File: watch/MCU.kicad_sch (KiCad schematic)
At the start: 14 parts, among them IC601 FAN5622SX, IC602 USBLC6-2P6, IC603 MX25U51245GZ4I00, IC604 NTS0104GU12, M601 NORA-B106, X603 Device, X608 Display

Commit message: Add speaker
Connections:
- net BMI270-INT: now also M601.E7 (P0.06/AIN2); no longer M601.G1 (P1.06)
- net LIS2MDL-INT: now also M601.F7 (P1.07); no longer M601.H7 (P0.29)
- net MIC-CLK: now also M601.G3 (P0.25/AIN4); no longer M601.F8 (P1.14)
- net MIC-DATA: now also M601.G2 (P0.26/AIN5); no longer M601.F9 (P1.15)
- net PA-BCLK: now also M601.C8 (P0.22); no longer M601.E7 (P0.06/AIN2)
- net Status: now also M601.E3 (P0.21); no longer M601.D3 (P0.07/AIN3)
- net VIB-EN: now also M601.G1 (P1.06); no longer M601.G2 (P0.26/AIN5)
- net ~{RESET_{HR}}: now also M601.D3 (P0.07/AIN3); no longer M601.E3 (P0.21)
- net ~{RTC-INT}: now also M601.F9 (P1.15); no longer M601.C8 (P0.22)
- no-connect marks 12 -> 10
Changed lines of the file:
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@@
 	)
 	(no_connect
-		(at 153.67 77.47)
-	)
-	(no_connect
-		(at 231.14 124.46)
-	)
-	(no_connect
 		(at 231.14 132.08)
 	)
@@
 	(wire
 		(pts
-			(xy 231.14 106.68) (xy 232.41 106.68)
+			(xy 153.67 77.47) (xy 154.94 77.47)
 		)
 		(stroke
@@
 	(wire
 		(pts
-			(xy 153.67 85.09) (xy 154.94 85.09)
+			(xy 231.14 104.14) (xy 232.41 104.14)
 		)
 		(stroke
@@
 	(wire
 		(pts
-			(xy 231.14 127) (xy 232.41 127)
+			(xy 153.67 125.73) (xy 154.94 125.73)
 		)
 		(stroke
@@
 	(wire
 		(pts
-			(xy 154.94 67.31) (xy 153.67 67.31)
+			(xy 232.41 124.46) (xy 231.14 124.46)
 		)
 		(stroke
@@
 	(wire
 		(pts
-			(xy 153.67 125.73) (xy 154.94 125.73)
+			(xy 153.67 85.09) (xy 154.94 85.09)
 		)
 		(stroke
@@
 	(wire
 		(pts
+			(xy 231.14 127) (xy 232.41 127)
+		)
+		(stroke
+			(width 0)
+			(type default)
+		)
+	)
+	(wire
+		(pts
 			(xy 109.22 106.68) (xy 109.22 109.22)
 		)
@@
 	(wire
 		(pts
-			(xy 231.14 104.14) (xy 232.41 104.14)
-		)
-		(stroke
-			(width 0)
-			(type default)
-		)
-	)
-	(wire
-		(pts
 			(xy 215.9 187.96) (xy 215.9 193.04)
 		)
@@
 	(hierarchical_label "PA-BCLK"
 		(shape output)
-		(at 154.94 125.73 0)
+		(at 154.94 85.09 0)
 		(effects
 			(font
@@
 	(hierarchical_label "MIC-DATA"
 		(shape input)
-		(at 232.41 104.14 0)
+		(at 154.94 74.93 0)
 		(effects
 			(font
@@
 	(hierarchical_label "~{RTC-INT}"
 		(shape input)
-		(at 154.94 85.09 0)
+		(at 232.41 104.14 0)
 		(effects
 			(font
@@
 	(hierarchical_label "~{RESET_{HR}}"
 		(shape output)
-		(at 154.94 87.63 0)
+		(at 154.94 123.19 0)
 		(effects
 			(font
@@
 	(hierarchical_label "Status"
 		(shape input)
-		(at 154.94 123.19 0)
+		(at 154.94 87.63 0)
 		(effects
 			(font
@@
 	(hierarchical_label "BMI270-INT"
 		(shape input)
-		(at 232.41 127 0)
+		(at 154.94 125.73 0)
 		(effects
 			(font
@@
 	(hierarchical_label "MIC-CLK"
 		(shape output)
-		(at 232.41 106.68 0)
+		(at 154.94 77.47 0)
 		(effects
 			(font
@@
 	(hierarchical_label "LIS2MDL-INT"
 		(shape input)
-		(at 154.94 67.31 0)
+		(at 232.41 124.46 0)
 		(effects
 			(font
@@
 	(hierarchical_label "VIB-EN"
 		(shape output)
-		(at 154.94 74.93 0)
+		(at 232.41 127 0)
 		(effects
 			(font

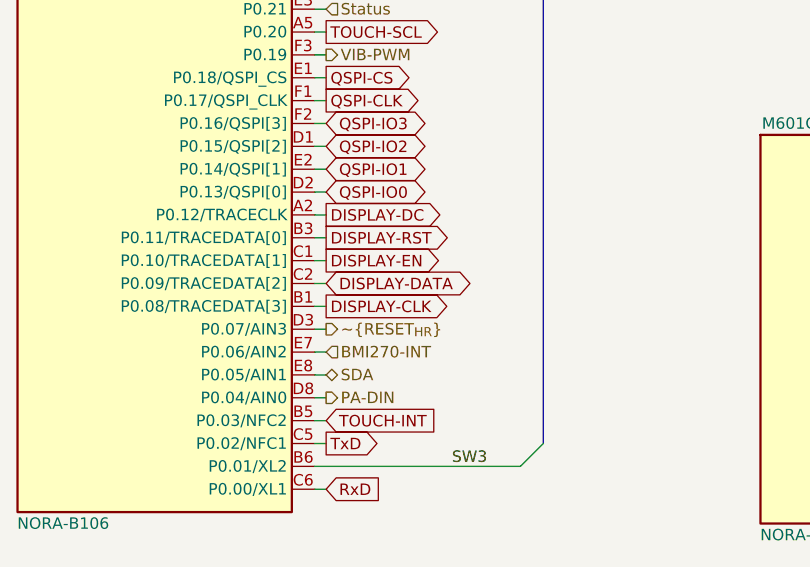
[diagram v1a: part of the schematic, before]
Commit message: Move display connector 3 mm to the outside and optimize routing
Signed-off-by: Daniel Kampert <DanielKampert@kampis-elektroecke.de>
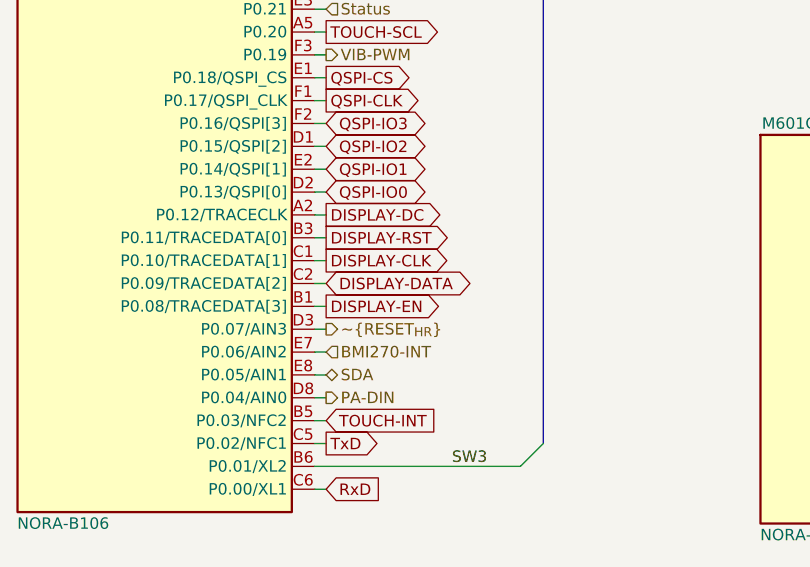
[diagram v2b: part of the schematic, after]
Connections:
- net DISPLAY-CLK: now also M601.C1 (P0.10/TRACEDATA[1]); no longer M601.B1 (P0.08/TRACEDATA[3])
- net DISPLAY-EN: now also M601.B1 (P0.08/TRACEDATA[3]); no longer M601.C1 (P0.10/TRACEDATA[1])
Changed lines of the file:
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@@
 	(global_label "DISPLAY-CLK"
 		(shape output)
-		(at 154.94 120.65 0)
-		(fields_autoplaced yes)
-		(effects
-			(font
-				(size 1.27 1.27)
-			)
-			(justify left)
-		)
-		(property "Intersheetrefs" "${INTERSHEET_REFS}"
-			(at 170.6253 120.65 0)
+		(at 154.94 115.57 0)
+		(fields_autoplaced yes)
+		(effects
+			(font
+				(size 1.27 1.27)
+			)
+			(justify left)
+		)
+		(property "Intersheetrefs" "${INTERSHEET_REFS}"
+			(at 170.6253 115.57 0)
 			(effects
 				(font
@@
 	(global_label "DISPLAY-EN"
 		(shape output)
-		(at 154.94 115.57 0)
-		(fields_autoplaced yes)
-		(effects
-			(font
-				(size 1.27 1.27)
-			)
-			(justify left)
-		)
-		(property "Intersheetrefs" "${INTERSHEET_REFS}"
-			(at 169.5367 115.57 0)
-			(effects
-				(font
+		(at 154.94 120.65 0)
+		(fields_autoplaced yes)
+		(effects
+			(font
+				(size 1.27 1.27)
+			)
+			(justify left)
+		)
+		(property "Intersheetrefs" "${INTERSHEET_REFS}"
+			(at 169.5367 120.65 0)
+			(effects
+				(font

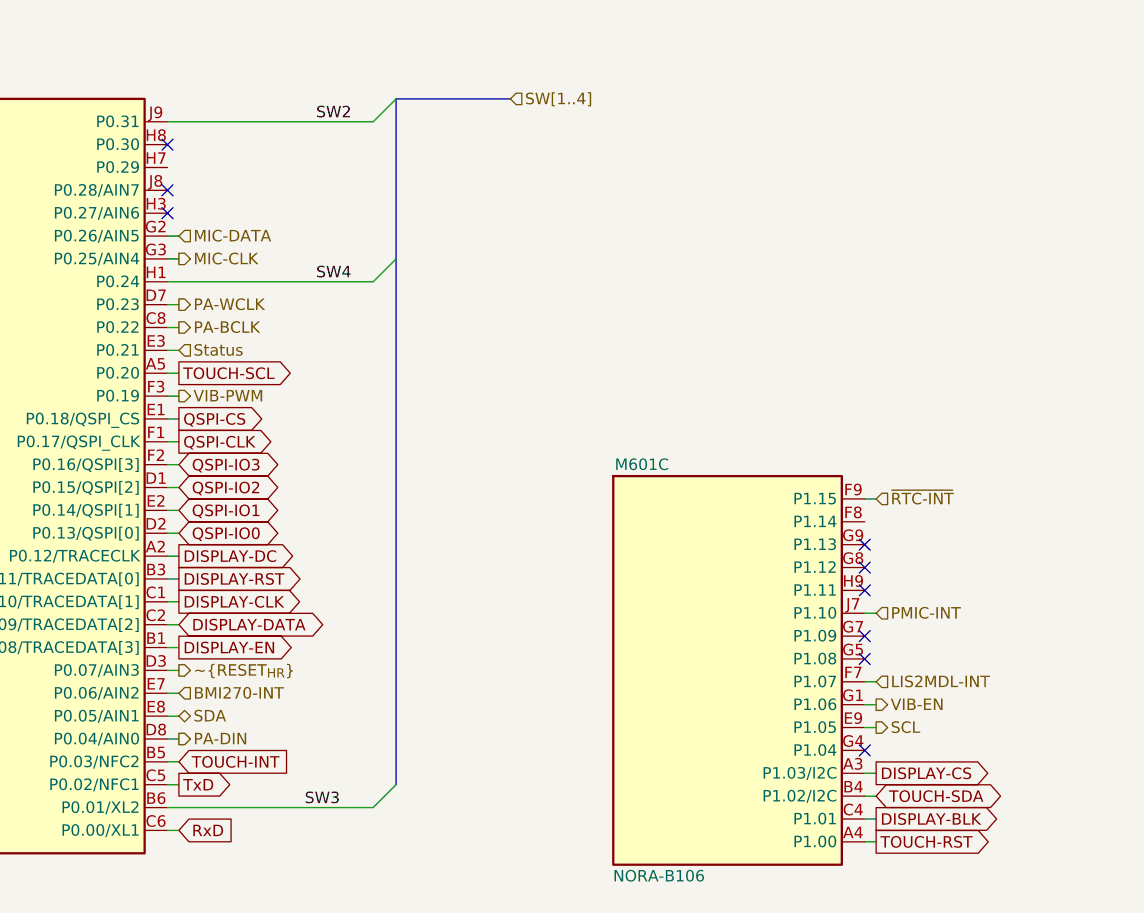
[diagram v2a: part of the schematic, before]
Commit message: Fix wrong Extension footprint
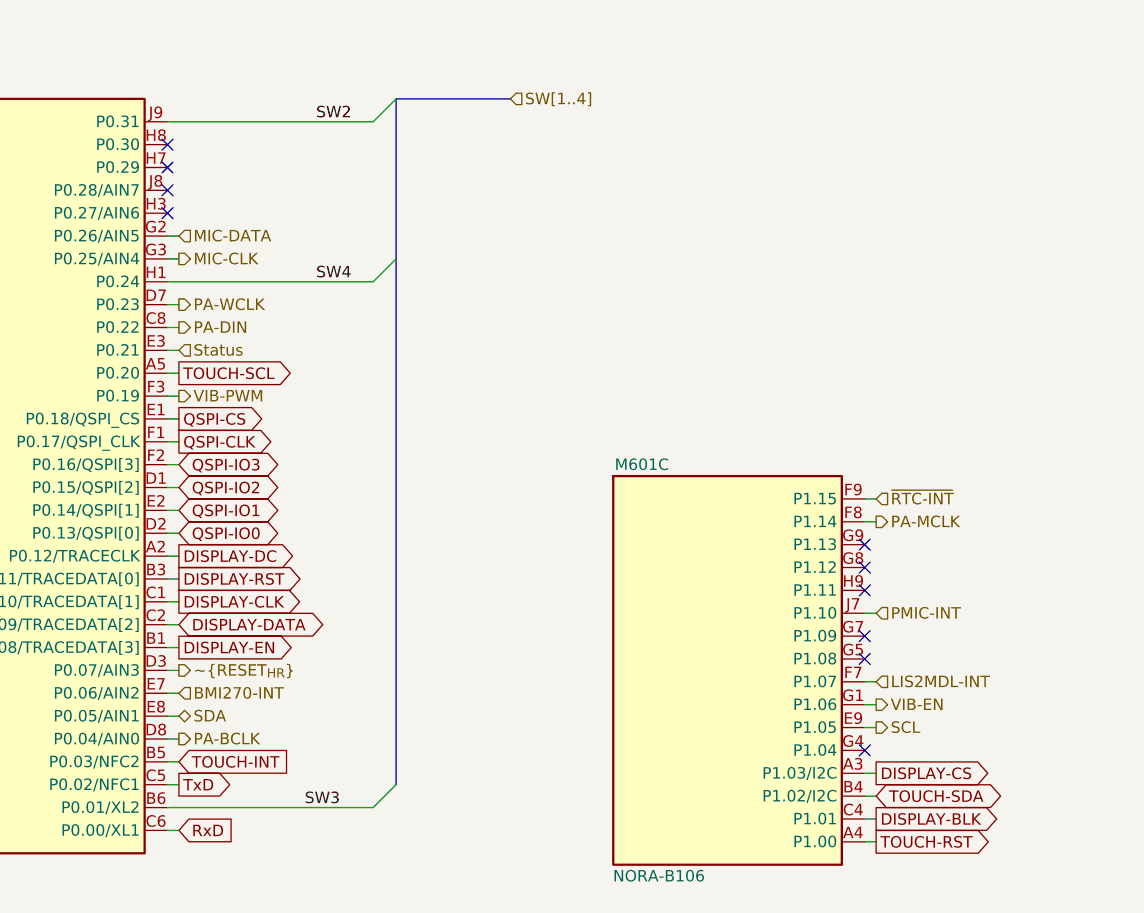
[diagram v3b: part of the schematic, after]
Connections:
- net PA-BCLK: now also M601.D8 (P0.04/AIN0); no longer M601.C8 (P0.22)
- net PA-DIN: now also M601.C8 (P0.22); no longer M601.D8 (P0.04/AIN0)
- net PA-MCLK: now reaches M601.F8 (P1.14)
- no-connect marks 10 -> 11
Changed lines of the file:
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@@
 	)
 	(no_connect
+		(at 153.67 67.31)
+	)
+	(no_connect
 		(at 231.14 114.3)
 	)
@@
 	(wire
 		(pts
+			(xy 231.14 124.46) (xy 232.41 124.46)
+		)
+		(stroke
+			(width 0)
+			(type default)
+		)
+	)
+	(wire
+		(pts
 			(xy 109.22 111.76) (xy 109.22 114.3)
 		)
@@
 	(wire
 		(pts
-			(xy 232.41 124.46) (xy 231.14 124.46)
+			(xy 232.41 106.68) (xy 231.14 106.68)
 		)
 		(stroke
@@
 	(hierarchical_label "PA-BCLK"
 		(shape output)
-		(at 154.94 85.09 0)
+		(at 154.94 130.81 0)
 		(effects
 			(font
@@
 		)
 	)
+	(hierarchical_label "PA-MCLK"
+		(shape output)
+		(at 232.41 106.68 0)
+		(effects
+			(font
+				(size 1.27 1.27)
+			)
+			(justify left)
+		)
+	)
 	(hierarchical_label "~{RTC-INT}"
 		(shape input)
@@
 	(hierarchical_label "PA-DIN"
 		(shape output)
-		(at 154.94 130.81 0)
+		(at 154.94 85.09 0)
 		(effects
 			(font

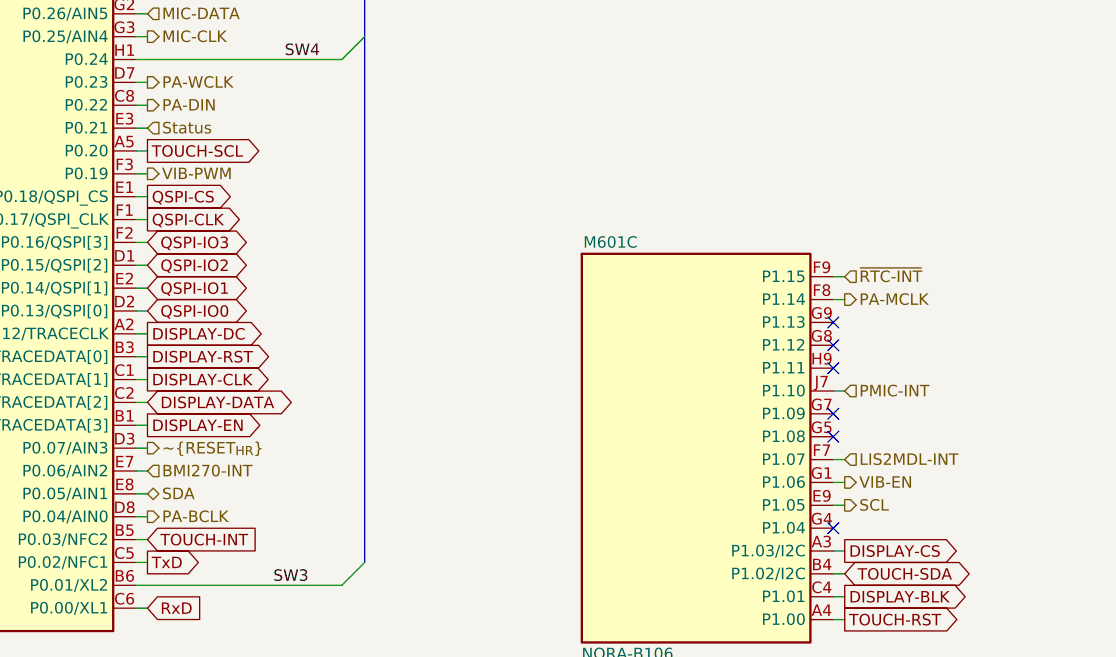
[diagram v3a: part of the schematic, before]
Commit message: New battery connector
- Add CI/CD workflow to check for changelog updates on pull requests

Signed-off-by: Daniel Kampert <DanielKampert|kampis-elektroecke.de>
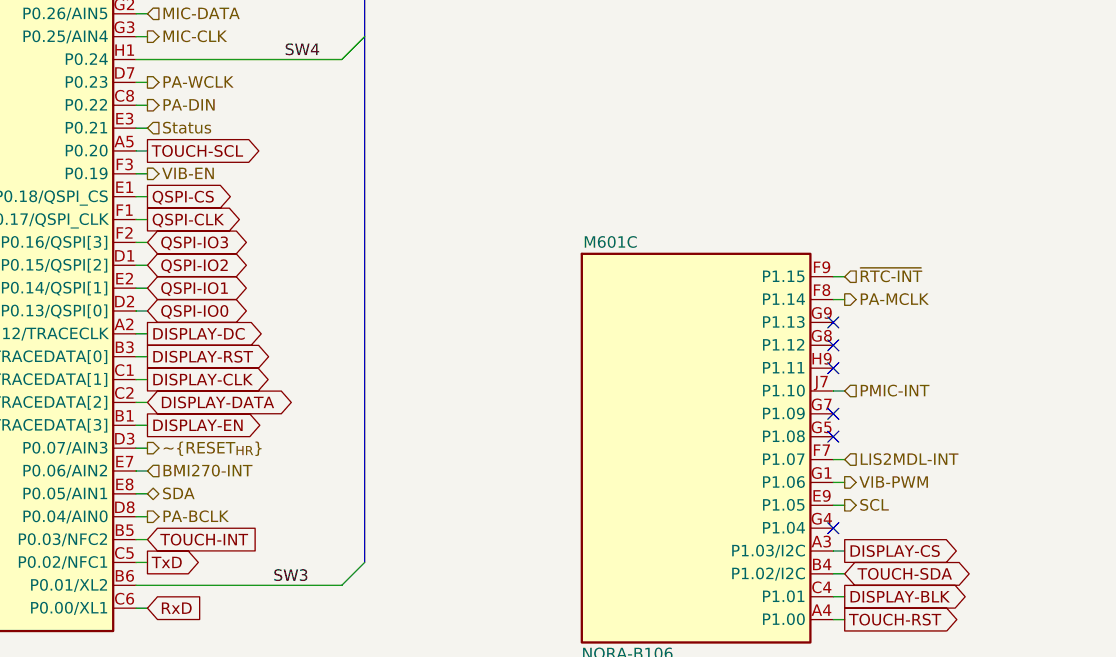
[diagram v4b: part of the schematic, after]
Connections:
- net VIB-EN: now also M601.F3 (P0.19); no longer M601.G1 (P1.06)
- net VIB-PWM: now also M601.G1 (P1.06); no longer M601.F3 (P0.19)
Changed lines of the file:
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@@
 	(hierarchical_label "VIB-EN"
 		(shape output)
-		(at 232.41 127 0)
+		(at 154.94 92.71 0)
 		(effects
 			(font
@@
 	(hierarchical_label "VIB-PWM"
 		(shape output)
-		(at 154.94 92.71 0)
+		(at 232.41 127 0)
 		(effects
 			(font

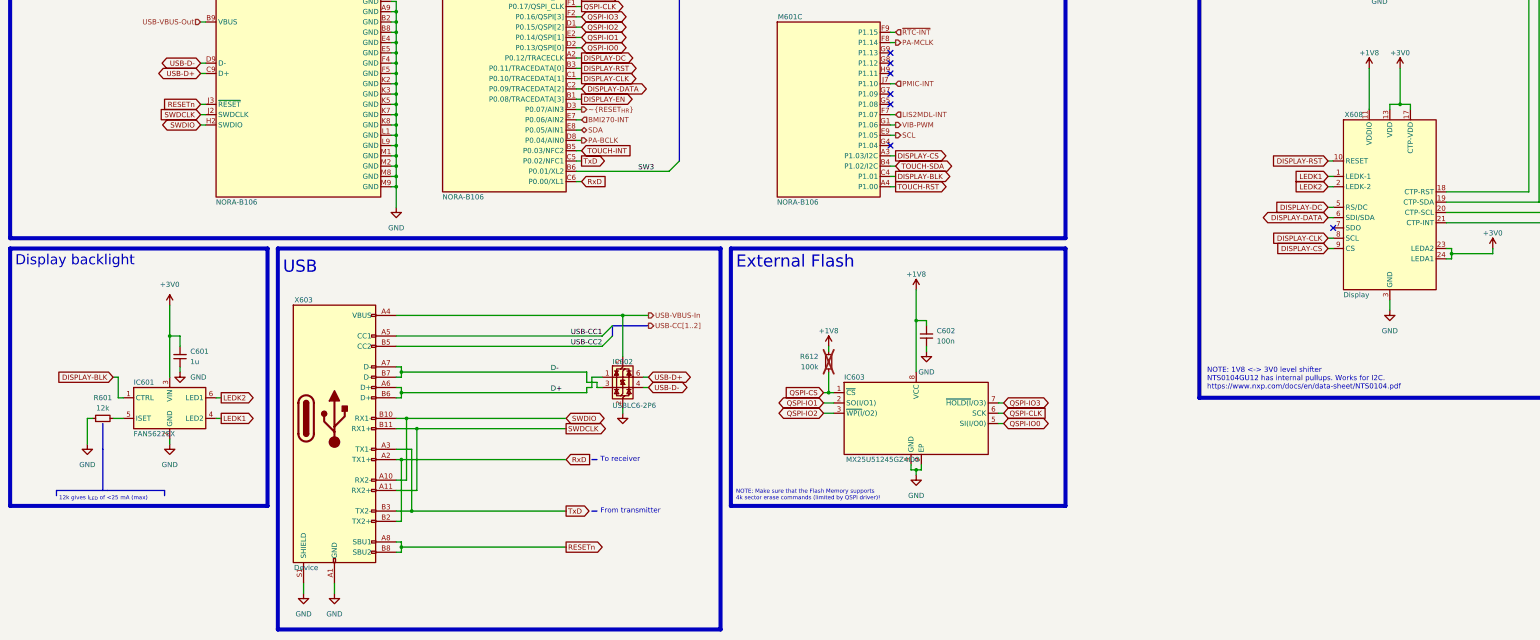
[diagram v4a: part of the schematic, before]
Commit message: Replace wrong extension connectors
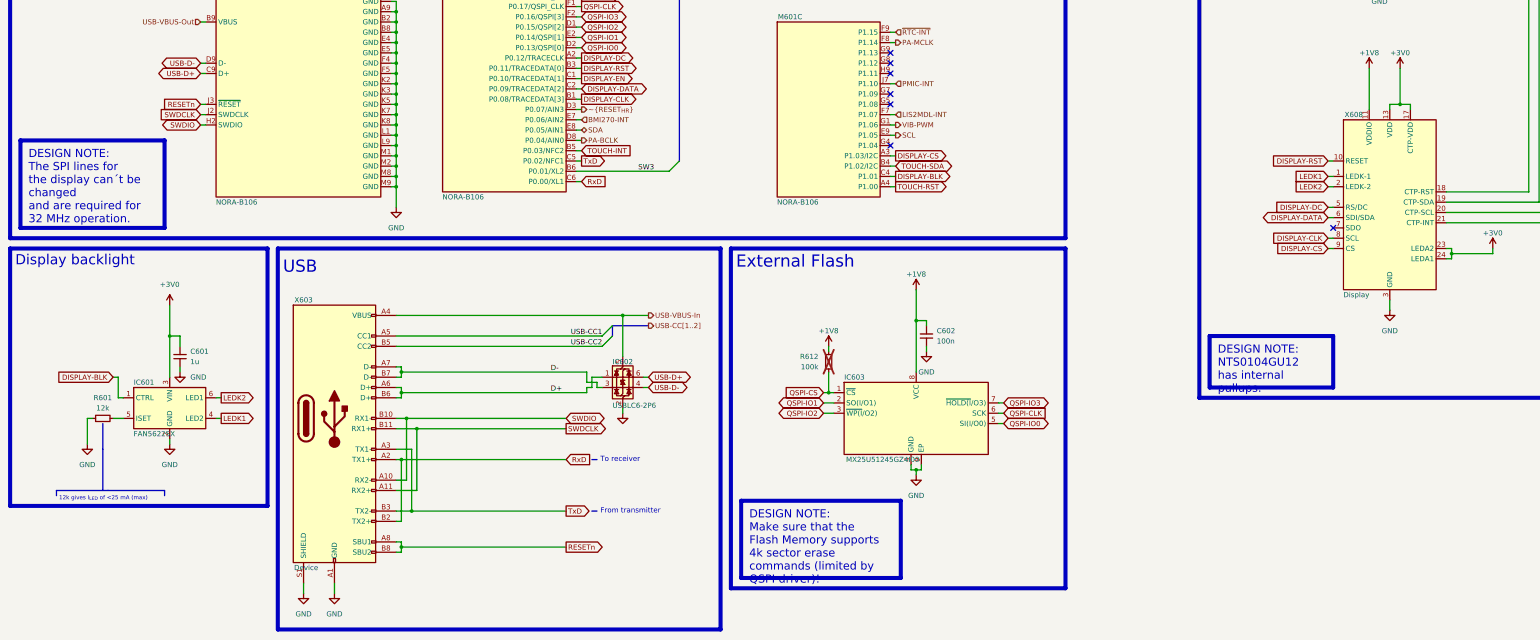
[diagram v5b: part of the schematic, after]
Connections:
- net DISPLAY-CLK: now also M601.B1 (P0.08/TRACEDATA[3]); no longer M601.C1 (P0.10/TRACEDATA[1])
- net DISPLAY-EN: now also M601.C1 (P0.10/TRACEDATA[1]); no longer M601.B1 (P0.08/TRACEDATA[3])
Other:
- note removed: "NOTE: 1V8 <-> 3V0 level shifter NTS0104GU12 has internal pullups. Works for I2C. https://www.nxp.com/docs/en/data-sheet/NTS0104.pdf"
- note removed: "NOTE: Make sure that the Flash Memory supports 4k sector erase commands (limited by QSPI driver)!"
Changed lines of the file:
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@@
 		)
 	)
-	(text "NOTE: Make sure that the Flash Memory supports\n4k sector erase commands (limited by QSPI driver)!"
-		(exclude_from_sim no)
-		(at 193.04 219.71 0)
-		(effects
-			(font
-				(size 1 1)
-			)
-			(justify left bottom)
-		)
-	)
 	(text "Display backlight"
 		(exclude_from_sim no)
@@
 		)
 	)
-	(text "NOTE: 1V8 <-> 3V0 level shifter\nNTS0104GU12 has internal pullups. Works for I2C.\nhttps://www.nxp.com/docs/en/data-sheet/NTS0104.pdf"
+	(text "Microcontroller\n(NORA-B106/nRF5340)"
 		(exclude_from_sim no)
-		(at 309.245 192.405 0)
+		(at 15.875 26.035 0)
 		(effects
 			(font
-				(size 1.27 1.27)
+				(size 3 3)
 			)
 			(justify left bottom)
 		)
 	)
-	(text "Microcontroller\n(NORA-B106/nRF5340)"
+	(text "External Flash"
 		(exclude_from_sim no)
-		(at 15.875 26.035 0)
+		(at 193.04 162.56 0)
 		(effects
 			(font
@@
 		)
 	)
-	(text "External Flash"
+	(text_box "DESIGN NOTE:\nNTS0104GU12 has internal pullups."
 		(exclude_from_sim no)
-		(at 193.04 162.56 0)
+		(at 309.88 179.07 0)
+		(size 30.48 12.7)
+		(margins 2 2 2 2)
+		(stroke
+			(width 1)
+			(type solid)
+			(color 200 200 200 1)
+		)
+		(fill
+			(type none)
+		)
 		(effects
 			(font
-				(size 3 3)
+				(face "Arial")
+				(size 2 2)
+				(color 0 0 0 1)
 			)
-			(justify left bottom)
+			(justify left top)
+		)
+	)
+	(text_box "DESIGN NOTE:\nMake sure that the Flash Memory supports\n4k sector erase commands (limited by QSPI driver)!"
+		(exclude_from_sim no)
+		(at 194.31 219.71 0)
+		(size 39.37 19.05)
+		(margins 2 2 2 2)
+		(stroke
+			(width 1)
+			(type solid)
+			(color 250 236 0 1)
+		)
+		(fill
+			(type none)
+		)
+		(effects
+			(font
+				(face "Arial")
+				(size 2 2)
+				(color 0 0 0 1)
+			)
+			(justify left top)
+		)
+	)
+	(text_box "DESIGN NOTE:\nThe SPI lines for the display can´t be changed\n and are required for 32 MHz operation."
+		(exclude_from_sim no)
+		(at 16.51 130.81 0)
+		(size 35.56 21.59)
+		(margins 2 2 2 2)
+		(stroke
+			(width 1)
+			(type solid)
+			(color 250 236 0 1)
+		)
+		(fill
+			(type none)
+		)
+		(effects
+			(font
+				(face "Arial")
+				(size 2 2)
+				(color 0 0 0 1)
+			)
+			(justify left top)
 		)
 	)
@@
 	(polyline
 		(pts
-			(xy 274.32 157.48) (xy 274.32 220.98)
+			(xy 274.32 157.48) (xy 274.32 241.3)
 		)
 		(stroke
@@
 	(polyline
 		(pts
-			(xy 191.77 157.48) (xy 191.77 220.98)
+			(xy 191.77 157.48) (xy 191.77 241.3)
 		)
 		(stroke
@@
 	(polyline
 		(pts
-			(xy 274.32 220.98) (xy 191.77 220.98)
+			(xy 274.32 241.3) (xy 191.77 241.3)
 		)
 		(stroke
@@
 	(global_label "DISPLAY-CLK"
 		(shape output)
-		(at 154.94 115.57 0)
+		(at 154.94 120.65 0)
 		(fields_autoplaced yes)
 		(effects
@@
 		)
 		(property "Intersheetrefs" "${INTERSHEET_REFS}"
-			(at 170.6253 115.57 0)
+			(at 170.6253 120.65 0)
 			(effects
 				(font
@@
 	(global_label "DISPLAY-EN"
 		(shape output)
-		(at 154.94 120.65 0)
+		(at 154.94 115.57 0)
 		(fields_autoplaced yes)
 		(effects
@@
 		)
 		(property "Intersheetrefs" "${INTERSHEET_REFS}"
-			(at 169.5367 120.65 0)
+			(at 169.5367 115.57 0)
 			(effects
 				(font
